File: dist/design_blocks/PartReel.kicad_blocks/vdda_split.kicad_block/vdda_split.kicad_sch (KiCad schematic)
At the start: 3 parts, among them U1 HT7333 3.3V

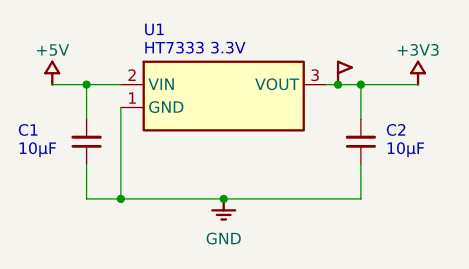
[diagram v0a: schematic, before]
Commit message: 디자인 블록 재배포: g431_min 0.2(VBAT 100nF C8), emi_power_in·buck_24v_5v P13 limit_mm 실측 보정 (boardworks g431_ind24 T2)
Co-Authored-By: Claude Fable 5 <noreply@anthropic.com>
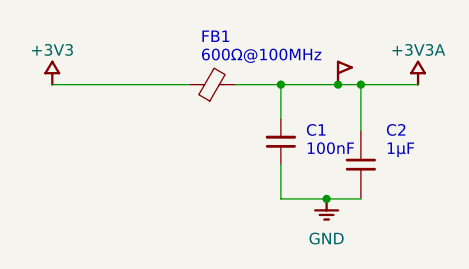
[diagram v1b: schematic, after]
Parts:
- removed C1, C2: 10µF, PCM_PartReel:antmicro_c3216x7r1h106k160ae, symbol PartReel:C_10u_50V_X7R_1206
- removed U1: HT7333 3.3V, PCM_PartReel:ht7333, symbol PartReel:ht7333
- added C1: 100nF, PCM_PartReel:antmicro_cl05a104ka5nnnc, symbol PartReel:C_100n_25V_0402
- added C2: 1µF, PCM_PartReel:samsung_cl05a105ka5nnnc, symbol PartReel:samsung_cl05a105ka5nnnc
- added FB1: 600Ω@100MHz, PCM_PartReel:antmicro_blm18ag601sn1d, symbol PartReel:FB_600Z_0.5A_Murata-BLM18AG_0603
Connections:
- net +3V3: now also FB1.1
- net GND: now also C1.1, C2.1
- new net +3V3A: C1.2, C2.2, FB1.2
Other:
- note added: "100nF"
- note added: "1µF"
- note added: "600Ω@100MHz"
- note added: "FB1"
- note removed: "10µF"
- note removed: "HT7333 3.3V"
- note removed: "U1"
- title: ldo_3v3 -> vdda_split
